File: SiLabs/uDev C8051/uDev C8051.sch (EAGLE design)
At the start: 17 parts, among them SW1 SPST.B3U-1000P(M), U1 C8051F387, U2 IP4221CZ6-S

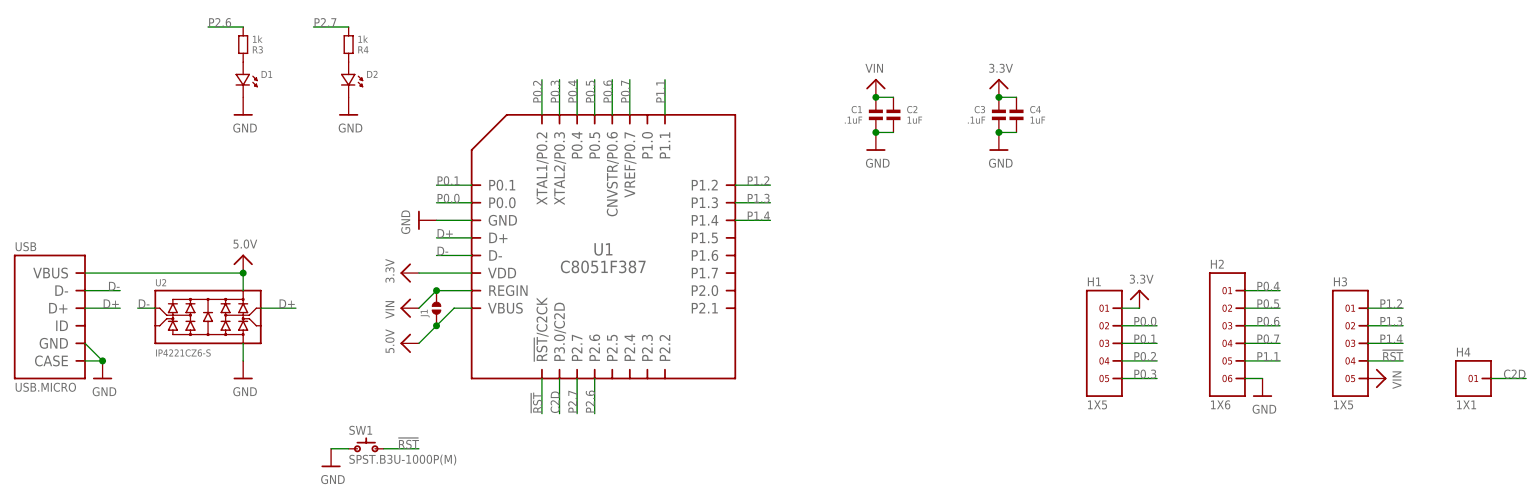
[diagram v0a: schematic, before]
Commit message: Completed uDev C8051 PCB (tiny as FUCK) Renamed files from F287 Trinket to uDev C8051
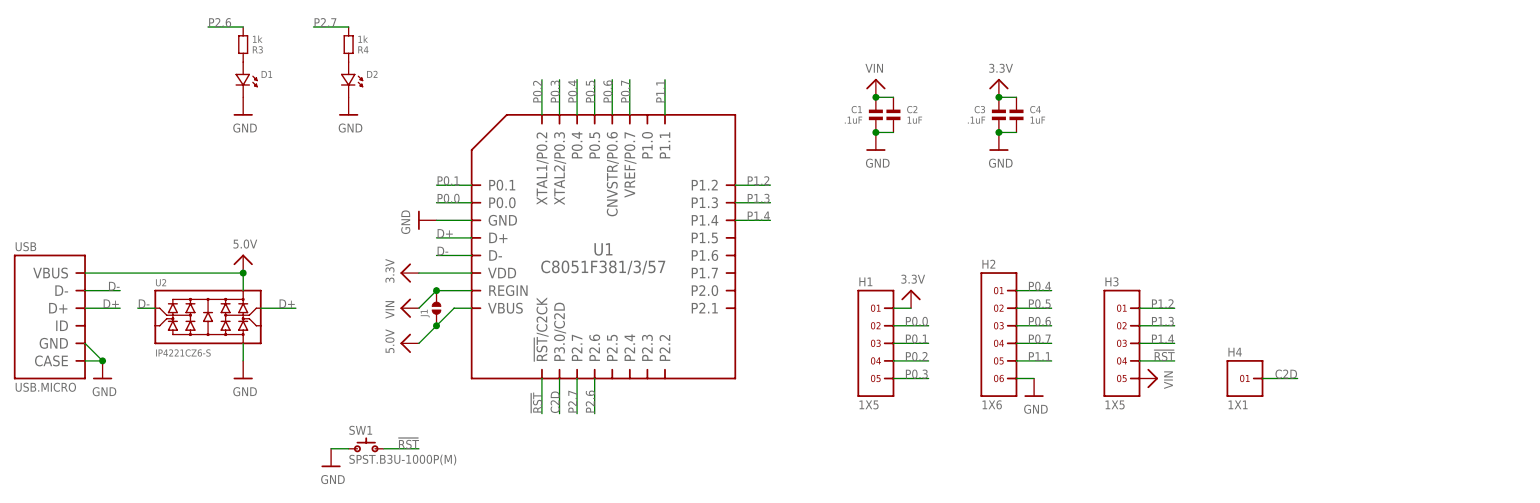
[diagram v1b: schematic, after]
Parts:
- U1: value C8051F387 -> C8051F381/3/57
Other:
- moved on the sheet: H1, H2, H3, H4
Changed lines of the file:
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@@
 <parts>
 <part name="FRAME1" library="microbuilder" deviceset="FRAME_A4" device=""/>
-<part name="U1" library="silabs" deviceset="C8051F381/3/5/7" device=".QFN" value="C8051F387"/>
+<part name="U1" library="silabs" deviceset="C8051F381/3/5/7" device=".QFN" value="C8051F381/3/57"/>
 <part name="U$3" library="microbuilder" deviceset="3.3V" device=""/>
 <part name="U$4" library="microbuilder" deviceset="GND" device=""/>
@@
 <instance part="R3" gate="G$1" x="48.26" y="144.78" rot="MR90"/>
 <instance part="R4" gate="G$1" x="63.5" y="144.78" rot="MR90"/>
-<instance part="U$8" gate="G$1" x="213.36" y="96.52" rot="MR90"/>
-<instance part="U$9" gate="G$1" x="177.8" y="109.22"/>
-<instance part="U$12" gate="G$1" x="195.58" y="93.98"/>
+<instance part="U$8" gate="G$1" x="180.34" y="96.52" rot="MR90"/>
+<instance part="U$9" gate="G$1" x="144.78" y="109.22"/>
+<instance part="U$12" gate="G$1" x="162.56" y="93.98"/>
 <instance part="U$13" gate="G$1" x="60.96" y="83.82"/>
 <instance part="C1" gate="G$1" x="139.7" y="134.62" rot="MR270"/>
@@
 <instance part="U2" gate="G$1" x="43.18" y="104.14"/>
 <instance part="U$2" gate="G$1" x="48.26" y="96.52"/>
-<instance part="H2" gate="G$1" x="190.5" y="101.6"/>
-<instance part="H1" gate="G$1" x="172.72" y="101.6"/>
-<instance part="H3" gate="G$1" x="208.28" y="101.6"/>
-<instance part="H4" gate="G$1" x="226.06" y="96.52"/>
+<instance part="H2" gate="G$1" x="157.48" y="101.6"/>
+<instance part="H1" gate="G$1" x="139.7" y="101.6"/>
+<instance part="H3" gate="G$1" x="175.26" y="101.6"/>
+<instance part="H4" gate="G$1" x="193.04" y="96.52"/>
 <instance part="U$10" gate="G$1" x="48.26" y="114.3"/>
 <instance part="U$18" gate="G$1" x="71.12" y="101.6" rot="R90"/>
@@
 <pinref part="H2" gate="G$1" pin="6"/>
 <pinref part="U$12" gate="G$1" pin="GND"/>
-<wire x1="193.04" y1="96.52" x2="195.58" y2="96.52" width="0.1524" layer="91"/>
+<wire x1="160.02" y1="96.52" x2="162.56" y2="96.52" width="0.1524" layer="91"/>
 </segment>
 <segment>
@@
 </segment>
 <segment>
-<wire x1="228.6" y1="96.52" x2="233.68" y2="96.52" width="0.1524" layer="91"/>
-<label x="233.68" y="96.52" size="1.27" layer="95" rot="MR0"/>
+<wire x1="195.58" y1="96.52" x2="200.66" y2="96.52" width="0.1524" layer="91"/>
+<label x="200.66" y="96.52" size="1.27" layer="95" rot="MR0"/>
 <pinref part="H4" gate="G$1" pin="1"/>
 </segment>
@@
 <segment>
 <pinref part="H3" gate="G$1" pin="4"/>
-<wire x1="215.9" y1="99.06" x2="210.82" y2="99.06" width="0.1524" layer="91"/>
-<label x="215.9" y="99.06" size="1.27" layer="95" rot="MR0"/>
+<wire x1="182.88" y1="99.06" x2="177.8" y2="99.06" width="0.1524" layer="91"/>
+<label x="182.88" y="99.06" size="1.27" layer="95" rot="MR0"/>
 </segment>
 </net>
@@
 <segment>
 <pinref part="U$9" gate="G$1" pin="3.3V"/>
-<wire x1="177.8" y1="106.68" x2="175.26" y2="106.68" width="0.1524" layer="91"/>
+<wire x1="144.78" y1="106.68" x2="142.24" y2="106.68" width="0.1524" layer="91"/>
 <pinref part="H1" gate="G$1" pin="1"/>
 </segment>
@@
 </segment>
 <segment>
-<wire x1="175.26" y1="104.14" x2="180.34" y2="104.14" width="0.1524" layer="91"/>
-<label x="180.34" y="104.14" size="1.27" layer="95" rot="MR0"/>
+<wire x1="142.24" y1="104.14" x2="147.32" y2="104.14" width="0.1524" layer="91"/>
+<label x="147.32" y="104.14" size="1.27" layer="95" rot="MR0"/>
 <pinref part="H1" gate="G$1" pin="2"/>
 </segment>
@@
 </segment>
 <segment>
-<wire x1="180.34" y1="101.6" x2="175.26" y2="101.6" width="0.1524" layer="91"/>
-<label x="180.34" y="101.6" size="1.27" layer="95" rot="MR0"/>
+<wire x1="147.32" y1="101.6" x2="142.24" y2="101.6" width="0.1524" layer="91"/>
+<label x="147.32" y="101.6" size="1.27" layer="95" rot="MR0"/>
 <pinref part="H1" gate="G$1" pin="3"/>
 </segment>
@@
 </segment>
 <segment>
-<wire x1="175.26" y1="99.06" x2="180.34" y2="99.06" width="0.1524" layer="91"/>
-<label x="180.34" y="99.06" size="1.27" layer="95" rot="MR0"/>
+<wire x1="142.24" y1="99.06" x2="147.32" y2="99.06" width="0.1524" layer="91"/>
+<label x="147.32" y="99.06" size="1.27" layer="95" rot="MR0"/>
 <pinref part="H1" gate="G$1" pin="4"/>
 </segment>
@@
 </segment>
 <segment>
-<wire x1="180.34" y1="96.52" x2="175.26" y2="96.52" width="0.1524" layer="91"/>
-<label x="180.34" y="96.52" size="1.27" layer="95" rot="MR0"/>
+<wire x1="147.32" y1="96.52" x2="142.24" y2="96.52" width="0.1524" layer="91"/>
+<label x="147.32" y="96.52" size="1.27" layer="95" rot="MR0"/>
 <pinref part="H1" gate="G$1" pin="5"/>
 </segment>
@@
 </segment>
 <segment>
-<wire x1="198.12" y1="109.22" x2="193.04" y2="109.22" width="0.1524" layer="91"/>
-<label x="198.12" y="109.22" size="1.27" layer="95" rot="MR0"/>
+<wire x1="165.1" y1="109.22" x2="160.02" y2="109.22" width="0.1524" layer="91"/>
+<label x="165.1" y="109.22" size="1.27" layer="95" rot="MR0"/>
 <pinref part="H2" gate="G$1" pin="1"/>
 </segment>
@@
 </segment>
 <segment>
-<wire x1="193.04" y1="106.68" x2="198.12" y2="106.68" width="0.1524" layer="91"/>
-<label x="198.12" y="106.68" size="1.27" layer="95" rot="MR0"/>
+<wire x1="160.02" y1="106.68" x2="165.1" y2="106.68" width="0.1524" layer="91"/>
+<label x="165.1" y="106.68" size="1.27" layer="95" rot="MR0"/>
 <pinref part="H2" gate="G$1" pin="2"/>
 </segment>
@@
 </segment>
 <segment>
-<wire x1="198.12" y1="104.14" x2="193.04" y2="104.14" width="0.1524" layer="91"/>
-<label x="198.12" y="104.14" size="1.27" layer="95" rot="MR0"/>
+<wire x1="165.1" y1="104.14" x2="160.02" y2="104.14" width="0.1524" layer="91"/>
+<label x="165.1" y="104.14" size="1.27" layer="95" rot="MR0"/>
 <pinref part="H2" gate="G$1" pin="3"/>
 </segment>
@@
 </segment>
 <segment>
-<wire x1="193.04" y1="101.6" x2="198.12" y2="101.6" width="0.1524" layer="91"/>
-<label x="198.12" y="101.6" size="1.27" layer="95" rot="MR0"/>
+<wire x1="160.02" y1="101.6" x2="165.1" y2="101.6" width="0.1524" layer="91"/>
+<label x="165.1" y="101.6" size="1.27" layer="95" rot="MR0"/>
 <pinref part="H2" gate="G$1" pin="4"/>
 </segment>
@@
 <segment>
 <pinref part="H3" gate="G$1" pin="3"/>
-<wire x1="210.82" y1="101.6" x2="215.9" y2="101.6" width="0.1524" layer="91"/>
-<label x="215.9" y="101.6" size="1.27" layer="95" rot="MR0"/>
+<wire x1="177.8" y1="101.6" x2="182.88" y2="101.6" width="0.1524" layer="91"/>
+<label x="182.88" y="101.6" size="1.27" layer="95" rot="MR0"/>
 </segment>
 </net>
@@
 <segment>
 <pinref part="H3" gate="G$1" pin="2"/>
-<wire x1="215.9" y1="104.14" x2="210.82" y2="104.14" width="0.1524" layer="91"/>
-<label x="215.9" y="104.14" size="1.27" layer="95" rot="MR0"/>
+<wire x1="182.88" y1="104.14" x2="177.8" y2="104.14" width="0.1524" layer="91"/>
+<label x="182.88" y="104.14" size="1.27" layer="95" rot="MR0"/>
 </segment>
 </net>
@@
 <segment>
 <pinref part="H3" gate="G$1" pin="1"/>
-<wire x1="210.82" y1="106.68" x2="215.9" y2="106.68" width="0.1524" layer="91"/>
-<label x="215.9" y="106.68" size="1.27" layer="95" rot="MR0"/>
+<wire x1="177.8" y1="106.68" x2="182.88" y2="106.68" width="0.1524" layer="91"/>
+<label x="182.88" y="106.68" size="1.27" layer="95" rot="MR0"/>
 </segment>
 </net>
@@
 <segment>
 <pinref part="H2" gate="G$1" pin="5"/>
-<wire x1="193.04" y1="99.06" x2="198.12" y2="99.06" width="0.1524" layer="91"/>
-<label x="198.12" y="99.06" size="1.27" layer="95" rot="MR0"/>
-</segment>
-<segment>
+<wire x1="160.02" y1="99.06" x2="165.1" y2="99.06" width="0.1524" layer="91"/>
+<label x="165.1" y="99.06" size="1.27" layer="95" rot="MR0"/>
+</segment>
+<segment>
